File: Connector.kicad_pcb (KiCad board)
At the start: 2 copper layers, 98 x 35 mm, 10 parts, among them J1 776163-1, J2 Conn_02x05_Top_Bottom, J3 Conn_02x04_Top_Bottom, J4 Conn_02x04_Top_Bottom, J5 Conn_02x05_Top_Bottom

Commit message: Rev A, New logo
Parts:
- removed the G*** at (172.0, 117.0)
- added G***: LOGO, MyLibrary:EVT_Logo, B.Cu at (171.2, 117.4)

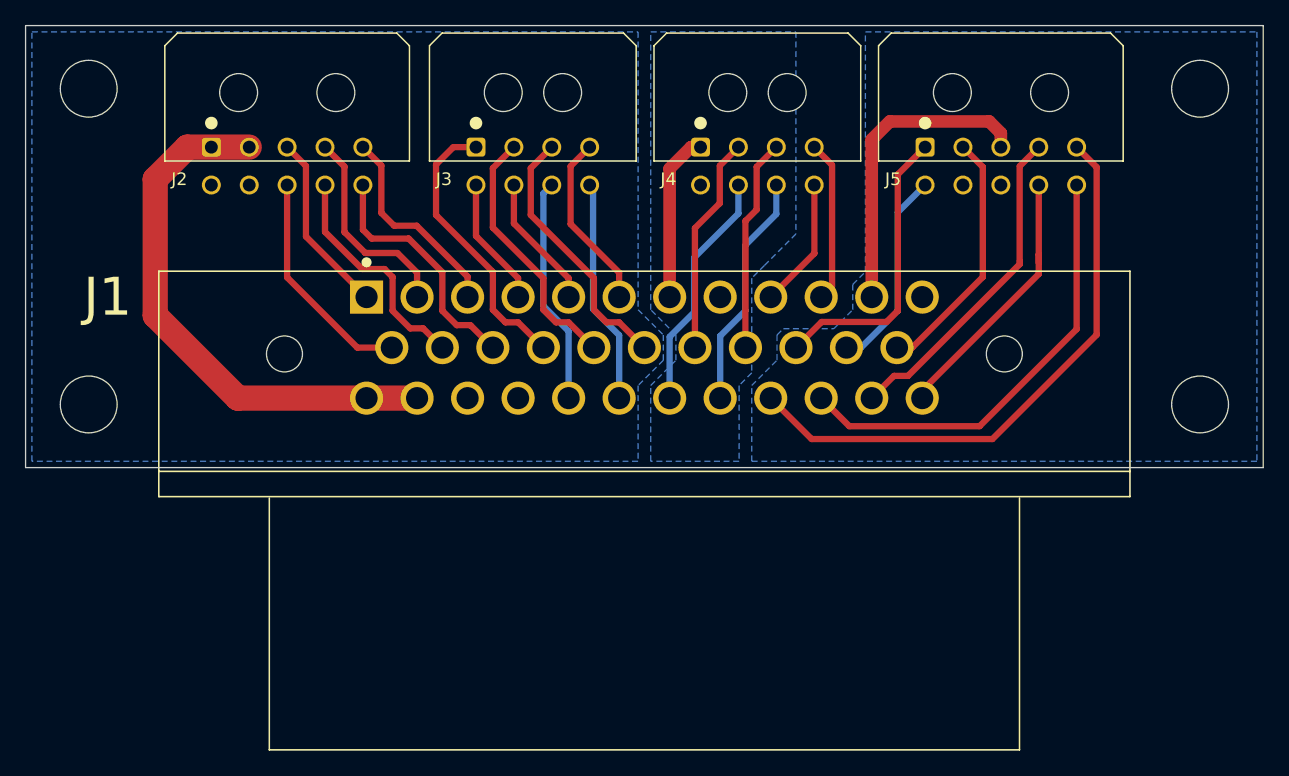
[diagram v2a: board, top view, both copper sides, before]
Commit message: Added rd_converter inputs/outputs
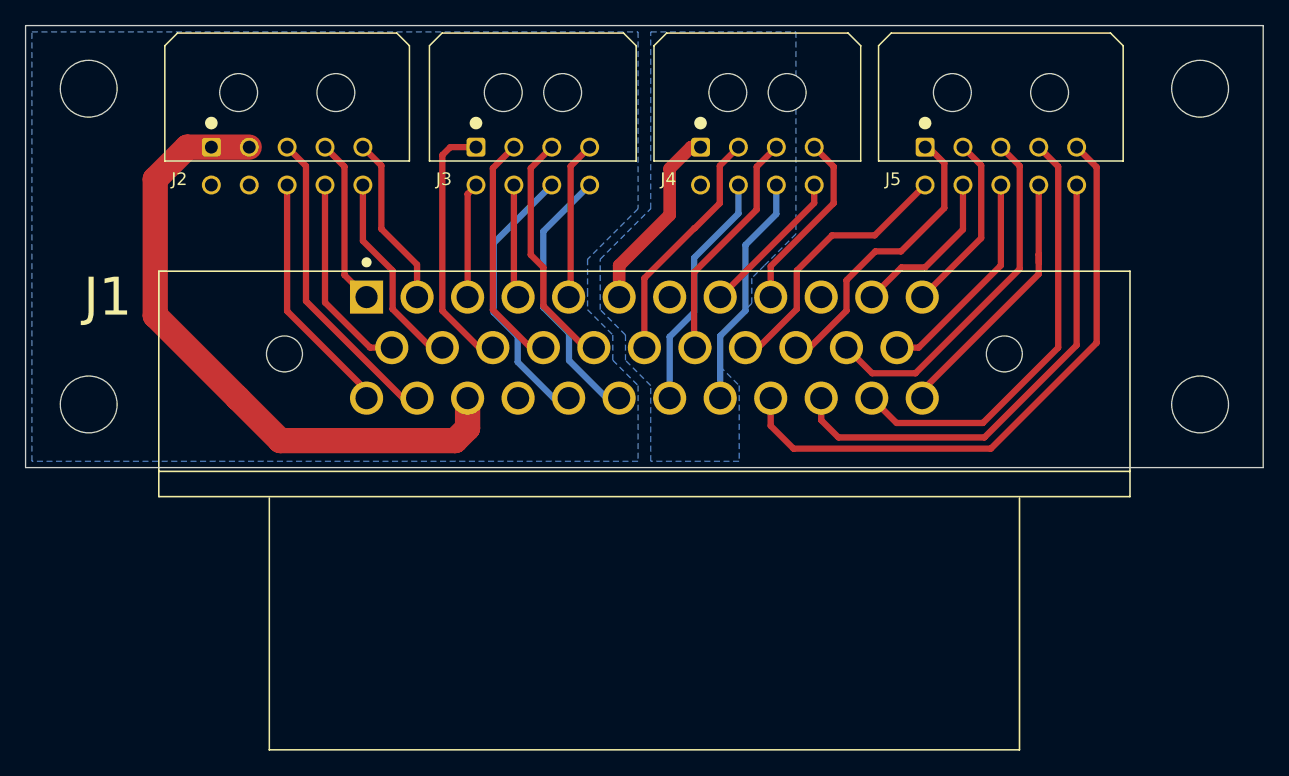
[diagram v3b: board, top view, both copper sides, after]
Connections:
- net /HALL_3 renamed /SIN
- J1 pad 1: /PowerSteeringPWM -> /ParkingBrake
- J1 pad 10: /CAN_L -> Net-(J1-Pad10)
- J1 pad 11: +5VD -> /COS_LO
- J1 pad 12: GNDD -> /COS
- J1 pad 13: /ShuntContactorOn -> /ReverseLight
- J1 pad 14: /ReverseLight -> /Pump
- J1 pad 15: /Pump -> /GearDrive
- J1 pad 16: /GearDrive -> /GearReverse
- J1 pad 17: /GearReverse -> /GearParking
- J1 pad 18: /GearParking -> /Brake_2
- J1 pad 19: /Brake_2 -> /Brake_1
- J1 pad 2: /ParkingBrake -> /PowerContactorOn
- J1 pad 20: /Brake_1 -> /SIN_LO
- J1 pad 22: /HALL_2 -> /~EXC_OUT
- J1 pad 23: /HALL_1 -> /EXC_OUT
- J1 pad 24: VDD -> /ShuntContactorOn
- J1 pad 25: VDD -> /PowerSteeringPWM
- J1 pad 26: GND -> VDD
- J1 pad 3: /PowerContactorOn -> /HighVoltageOn
- J1 pad 32: /NTC_AW_2 -> /NTC_FW_2
- J1 pad 33: /NTC_AW_1 -> /NTC_FW_1
- J1 pad 34: /NTC_FW_2 -> /NTC_AW_2
- J1 pad 35: /NTC_FW_1 -> /NTC_AW_1
- J1 pad 4: /HighVoltageOn -> /IgnitionOn
- J1 pad 5: /IgnitionOn -> /EmergencyStop
- J1 pad 6: /EmergencyStop -> +5VA
- J1 pad 7: +5VA -> GNDA
- J1 pad 8: GNDA -> /CAN_H
- J1 pad 9: /CAN_H -> /CAN_L
- J5 pad 10: /NTC_AW_1 -> /NTC_FW_1
- J5 pad 2: /HALL_1 -> /COS
- J5 pad 3: +5VD -> /~EXC_OUT
- J5 pad 4: /NTC_FW_2 -> /NTC_AW_2
- J5 pad 5: /NTC_AW_2 -> /NTC_FW_2
- J5 pad 6: /HALL_2 -> /SIN_LO
- J5 pad 7: GNDD -> /COS_LO
- J5 pad 8: GNDD -> /EXC_OUT
- J5 pad 9: /NTC_FW_1 -> /NTC_AW_1
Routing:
- net /~EXC_OUT: track 0.00 -> 28.2 mm
- net +5VD: track 24.8 -> 0.00 mm
- net /NTC_FW_2: track 26.0 -> 48.4 mm
- net /SIN_LO: track 0.00 -> 21.3 mm
- net /HALL_1: track 20.0 -> 0.00 mm
- net /EXC_OUT: track 0.00 -> 17.3 mm
- net /HALL_2: track 17.1 -> 0.00 mm
- net /NTC_FW_1: track 21.5 -> 38.2 mm
- net /COS: track 0.00 -> 14.4 mm
- net /NTC_AW_1: track 35.7 -> 21.5 mm
- net /COS_LO: track 0.00 -> 13.0 mm
- net /NTC_AW_2: track 46.1 -> 34.6 mm
- net /PowerSteeringPWM: track 14.5 -> 24.8 mm
- net VDD: track 42.7 -> 50.9 mm
- net /RightSupport: track 18.0 -> 21.9 mm
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- removed copper zone on B.Cu, net GNDD
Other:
- board text added: "Rev B"
- board text removed: "Rev A"
